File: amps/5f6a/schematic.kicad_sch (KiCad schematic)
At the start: 64 parts, among them T3 2R sec

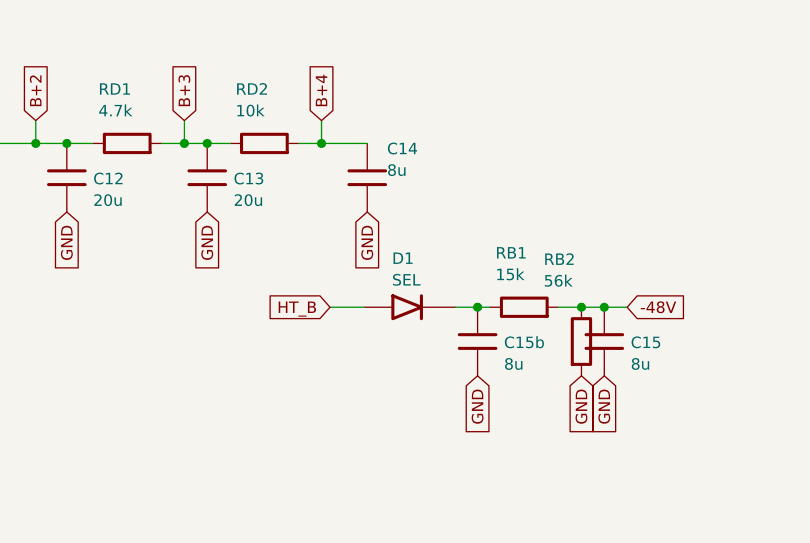
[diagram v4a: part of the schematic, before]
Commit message: Fix: 17 bias rectifiers and six HT diodes drawn backwards; the 6G6-B and 6G4 bias rows as their drawings show; AA1164 V4 units
Rectifier polarity has no gate. The netlists model every supply as an ideal
source, the sheet-vs-board check treats a two-terminal part as unordered, and
the boards' `cathode:` fields were copied from the sheets. Measured over all
68 diodes on 40 sheets: 18 negative-bias rectifiers had the cathode on the
negative node (a diode that way round would charge the node POSITIVE), and all
six 6G6-B HT diodes pointed away from B+. The printed negative bias on each of
those sheets falsifies the drawn orientation; the nine bias rectifiers already
right (AA1164, AA864, AB165, B15N, DR103, JTM100, M1959, M2204, 6G6-B) show
the idiom. Flipped: 5E4-A, 5E5-A, 5E6-A, 5F10, 5F4, 5F6, 5F6-A, 5F8-A, 5G9,
6G2, 6G3, 6G4, 6G5, AA964, AB763, AB763 Super, AB763 Twin, JTM45 (the
M1987's is with the Marshall board repair) and the 6G6-B's DR1-DR6. The
5F8-A board, which had copied its sheet, has the band moved to the tap side;
the other boards' bands are with the board-repair wave. A gate is next.

6G6-B bias. E-FB (6431x3364): the 1K 1W rises from TR1's SECOND secondary
terminal, a bias tap between the upper HT end and the grounded centre tap,
to the diode's + end. The sheet fed the diode from the HT end with the 1K
after it. T1 now carries its tap pin and the row reads tap -> 1K -> diode ->
-54 V. (The triage had read "HT end"; the native crop shows the tap.)

6G4 bias. A-FJ, read natively: tap -> rectifier -> 8 uF -> 10K -> the -55 V
node, which carries a second 8 uF and the 56K to ground as a bleeder. The
sheet fed the rectifier from an HT end, drew the 56K in series and carried
one capacitor. CBIAS2 joins the parts list, and RBIAS1's role now says
bleeder.

AA1164 V4. The K-FD sheet prints the phase inverter 7/6/8 and the tremolo
oscillator 2/1/3 (5554x4346); the sheet had them the other way round.

Gates: check_schematics 40/0 (+selftest), verify_schematic_nets 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
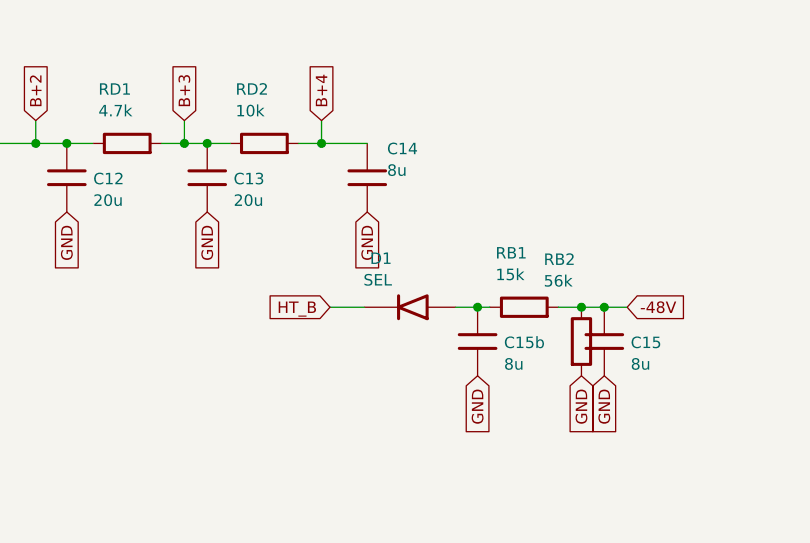
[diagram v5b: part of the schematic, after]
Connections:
- net HT_B: now also D1.2 (K); no longer D1.1 (A)
- net at C15b.1, RB1.1: now also D1.1 (A); no longer D1.2 (K)
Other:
- moved on the sheet: D1
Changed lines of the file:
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@@
   (wire (pts (xy 131.709 142.278) (xy 135.519 142.278))
     (stroke (width 0) (type default)))
-  (symbol (lib_id "cx:DIODE_SS") (at 140.599 142.278 0) (unit 1)
+  (symbol (lib_id "cx:DIODE_SS") (at 140.599 142.278 180) (unit 1)
     (in_bom yes) (on_board yes)
     (property "Reference" "D1" (at 138.599 136.878 0) (effects (font (size 1.27 1.27)) (justify left)))

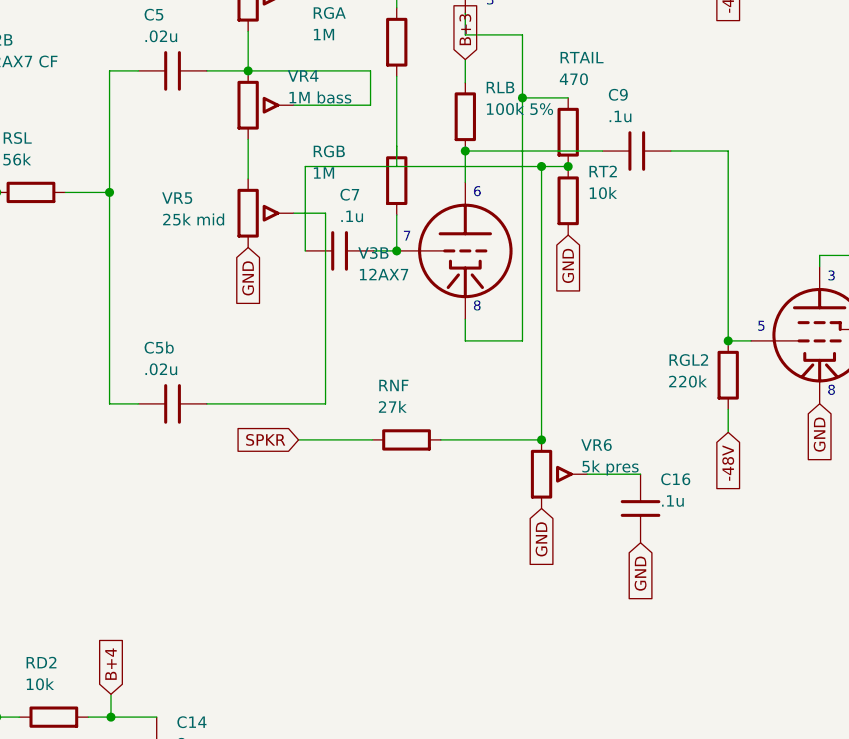
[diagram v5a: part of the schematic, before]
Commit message: Fix: 5F6-A tail returns through the feedback/presence node, not to ground, as I-EG draws it; its two printed tail figures are disputed
- I-EG schematic (6412 x 3947, crops (3100,700)-(3800,2400) and
  (5300,700)-(6412,2500)): the 10k (RT2) leaves the tail junction for a
  vertical of its own carrying the 27k feedback resistor from the speaker, the
  V3B grid's .1-200 and the top of the 5k presence track, whose lower lug is
  grounded with its .1-200 wiper cap to ground. I-EG layout (6402 x 3641, crops
  (3380,1380)-(4450,2400), (2419,534)-(4019,2846)): the same node is the 10k's
  top eyelet with the .1/200 cap, joined under the board to the 27k's eyelet and
  the presence lead, separate from the grounded eyelet beside it.
- Netlist: RT2 JPI PRES; RNF PRES 0 27k (the OT secondary is DC ground);
  RPRES PRES 0 5k; C7 GPIB PRES now modelled. It grounded RT2, dropped the two
  returns as "DC-neutral", and said "the printed chart (J +32.5 V = Itail x 10k)
  confirms this reading" -- arithmetic establishing a reading. Gone.
- Sheet: RT2's foot runs straight down to the node; RNF, VR6 and C7 moved off J
  onto it (C7 now hangs below the V3B grid). sch_map element_pins RPRES =
  VR6.1/VR6.3.
- Board: RT2.b no longer drops to the bus; it carries RNF.b, VR6.lug3 and C7.b.
  C7 is placed on the board at [0,22]-[0,23], as the factory board places it
  (it was absent: a sheet-only row); RPRES declared netlist_unplaced. The
  factory board also mounts the 27k beside the 10k; with no free eyelet pair it
  stays drawn at the speaker jacks, and the caption and BOM notes now say so
  (they called it chassis wiring).
- Chart: with the drawn tail KPI 32.2 -> 43.7 V and JPI 30.7 -> 42.3 V against
  printed 34 / 32.5. The printed plates imply 3.38 mA; x 10k = 33.8 V fits only
  a grounded foot, and the chart is figure for figure the 5F6's, whose 10k is
  grounded. Both nodes are disputed with that arithmetic, not force-fitted.
  PRES added as informational (12.6 V).
- VERIFIED facts cha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
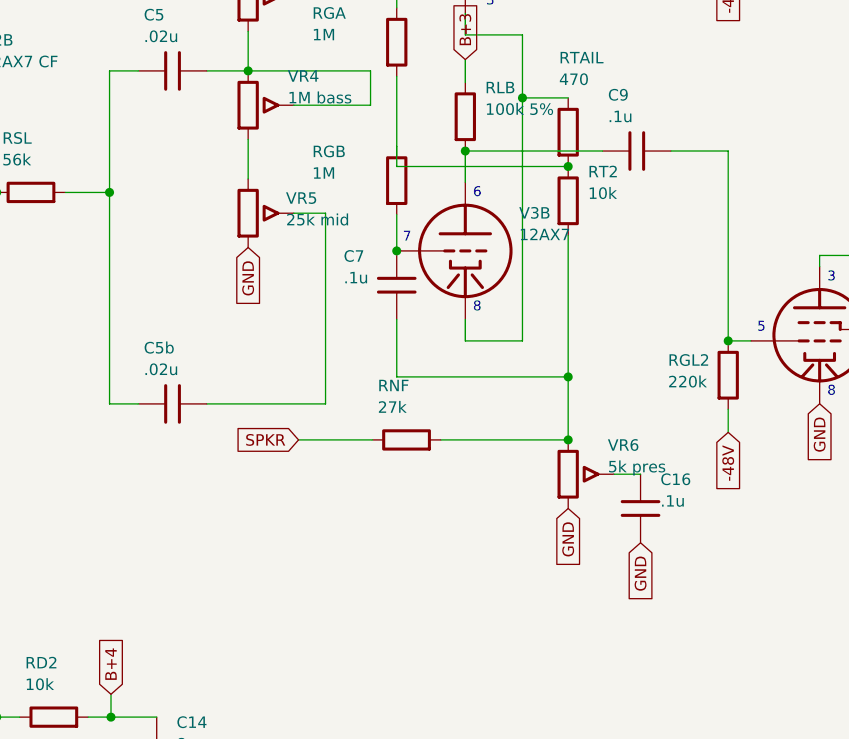
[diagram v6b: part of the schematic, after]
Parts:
- removed C15: 8u, symbol cx:C
- removed C16: .1u, symbol cx:C
- removed RGL1, RGL2: 220k, symbol cx:R
- added C8, C9: .1u, symbol cx:C
- added RB2: 56k, symbol cx:R
- added VR6: 5k pres, symbol cx:POT
- C15: renamed from RB2; value 56k -> 8u; symbol cx:R -> cx:C
- C16: renamed from VR6; value 5k pres -> .1u; symbol cx:POT -> cx:C
- RGL1: renamed from V4; value 5881 -> 220k; symbol cx:PENTODE -> cx:R
- RGL2: renamed from V5; value 5881 -> 220k; symbol cx:PENTODE -> cx:R
- V4: renamed from C8; value .1u -> 5881; symbol cx:C -> cx:PENTODE
- V5: renamed from C9; value .1u -> 5881; symbol cx:C -> cx:PENTODE
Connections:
- net -48V: now also RGL1.2, RGL2.2, RB2.1
- net GND: now also C16.2, V4.4 (K), V5.4 (K), RB2.2, VR6.3; no longer C16.3, RGL1.4 (K), RGL2.4 (K), RT2.2
- net at RS2.1: now also V5.3 (G2); no longer RGL2.3 (G2)
- net at RLB.2, V3B.1 (P): now also C9.1; no longer V5.1
- net at V5.2 (G1): now also RGL2.1, C9.2; no longer RGL2.2 (G1)
- net at RLA.2, V3A.1 (P): now also C8.1; no longer V4.1
- net at V4.2 (G1): now also RGL1.1, C8.2; no longer RGL1.2 (G1)
- net at T3.1 (PRI_A): now also V4.1 (P); no longer RGL1.1 (P)
- net at RS1.1: now also V4.3 (G2); no longer RGL1.3 (G2)
- net at RGA.2, RGB.1, RT2.1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: no longer C16.1, C7.1, RNF.2
- net at T3.3 (PRI_B): now also V5.1 (P); no longer RGL2.1 (P)
- net at RGB.2, V3B.2 (G): now also C7.1; no longer C7.2
- new net: C7.2, RNF.2, RT2.2, VR6.1
- new net: C16.1, VR6.2 (W)
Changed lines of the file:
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@@
   (symbol (lib_id "cx:POT") (at 146.009 68.088 0) (unit 1)
     (in_bom yes) (on_board yes)
-    (property "Reference" "VR5" (at 136.437 66.448 0) (effects (font (size 1.27 1.27)) (justify left)))
-    (property "Value" "25k mid" (at 136.437 68.848 0) (effects (font (size 1.27 1.27)) (justify left))))
+    (property "Reference" "VR5" (at 150.211 66.448 0) (effects (font (size 1.27 1.27)) (justify left)))
+    (property "Value" "25k mid" (at 150.211 68.848 0) (effects (font (size 1.27 1.27)) (justify left))))
   (global_label "GND" (shape input) (at 146.009 71.898 270)
     (effects (font (size 1.27 1.27)) (justify right)))
@@
   (symbol (lib_id "cx:TRIODE") (at 170.139 72.278 0) (unit 1)
     (in_bom yes) (on_board yes)
-    (property "Reference" "V3B" (at 158.234 72.558 0) (effects (font (size 1.27 1.27)) (justify left)))
-    (property "Value" "12AX7" (at 158.234 74.958 0) (effects (font (size 1.27 1.27)) (justify left)))
-    (property "Basing_unit" "1" (at 158.234 77.358 0) (effects (font (size 1.27 1.27)) hide)))
+    (property "Reference" "V3B" (at 176.119 68.098 0) (effects (font (size 1.27 1.27)) (justify left)))
+    (property "Value" "12AX7" (at 176.119 70.498 0) (effects (font (size 1.27 1.27)) (justify left)))
+    (property "Basing_unit" "1" (at 176.119 72.898 0) (effects (font (size 1.27 1.27)) hide)))
   (wire (pts (xy 170.139 30.658) (xy 170.139 27.178))
     (stroke (width 0) (type default)))
@@
     (property "Reference" "RT2" (at 183.769 63.508 0) (effects (font (size 1.27 1.27)) (justify left)))
     (property "Value" "10k" (at 183.769 65.908 0) (effects (font (size 1.27 1.27)) (justify left))))
-  (global_label "GND" (shape input) (at 181.569 70.518 270)
-    (effects (font (size 1.27 1.27)) (justify right)))
   (wire (pts (xy 162.519 38.278) (xy 162.519 45.278))
     (stroke (width 0) (type default)))
@@
   (wire (pts (xy 162.519 60.658) (xy 162.519 62.898))
     (stroke (width 0) (type default)))
-  (wire (pts (xy 162.519 62.898) (xy 178.609 62.898))
-    (stroke (width 0) (type default)))
-  (wire (pts (xy 178.609 62.898) (xy 181.569 62.898))
+  (wire (pts (xy 162.519 62.898) (xy 181.569 62.898))
     (stroke (width 0) (type default)))
   (wire (pts (xy 162.519 72.278) (xy 162.519 68.278))
@@
     (property "Reference" "RGB" (at 153.119 61.268 0) (effects (font (size 1.27 1.27)) (justify left)))
     (property "Value" "1M" (at 153.119 63.668 0) (effects (font (size 1.27 1.27)) (justify left))))
-  (symbol (lib_id "cx:C") (at 156.169 72.278 90) (unit 1)
+  (symbol (lib_id "cx:C") (at 162.519 76.088 0) (unit 1)
     (in_bom yes) (on_board yes)
-    (property "Reference" "C7" (at 156.169 66.078 270) (effects (font (size 1.27 1.27)) (justify left)))
-    (property "Value" ".1u" (at 156.169 68.478 270) (effects (font (size 1.27 1.27)) (justify left))))
-  (wire (pts (xy 159.979 72.278) (xy 162.519 72.278))
+    (property "Reference" "C7" (at 156.619 72.888 0) (effects (font (size 1.27 1.27)) (justify left)))
+    (property "Value" ".1u" (at 156.619 75.288 0) (effects (font (size 1.27 1.27)) (justify left))))
+  (wire (pts (xy 162.519 79.898) (xy 162.519 86.278))
     (stroke (width 0) (type default)))
-  (wire (pts (xy 152.359 72.278) (xy 152.359 72.278))
+  (wire (pts (xy 162.519 86.278) (xy 181.569 86.278))
     (stroke (width 0) (type default)))
-  (wire (pts (xy 152.359 72.278) (xy 152.359 62.898))
+  (wire (pts (xy 181.569 70.518) (xy 181.569 86.278))
     (stroke (width 0) (type default)))
-  (wire (pts (xy 152.359 62.898) (xy 162.519 62.898))
+  (wire (pts (xy 181.569 86.278) (xy 181.569 93.278))
     (stroke (width 0) (type default)))
-  (junction (at 178.609 62.898) (diameter 1.001) (color 0 0 0 0))
-  (wire (pts (xy 178.609 62.898) (xy 178.609 93.278))
-    (stroke (width 0) (type default)))
-  (junction (at 178.609 93.278) (diameter 1.001) (color 0 0 0 0))
+  (junction (at 181.569 86.278) (diameter 1.001) (color 0 0 0 0))
+  (junction (at 181.569 93.278) (diameter 1.001) (color 0 0 0 0))
   (symbol (lib_id "cx:R") (at 163.609 93.278 90) (unit 1)
     (in_bom yes) (on_board yes)
     (property "Reference" "RNF" (at 160.409 87.278 270) (effects (font (size 1.27 1.27)) (justify left)))
     (property "Value" "27k" (at 160.409 89.678 270) (effects (font (size 1.27 1.27)) (justify left))))
-  (wire (pts (xy 167.419 93.278) (xy 178.609 93.278))
+  (wire (pts (xy 167.419 93.278) (xy 181.569 93.278))
     (stroke (width 0) (type default)))
   (wire (pts (xy 151.609 93.278) (xy 159.799 93.278))
@@
   (global_label "SPKR" (shape input) (at 151.609 93.278 180)
     (effects (font (size 1.27 1.27)) (justify right)))
-  (symbol (lib_id "cx:POT") (at 178.609 97.088 0) (unit 1)
+  (symbol (lib_id "cx:POT") (at 181.569 97.088 0) (unit 1)
     (in_bom yes) (on_board yes)
-    (property "Reference" "VR6" (at 183.009 93.888 0) (effects (font (size 1.27 1.27)) (justify left)))
-    (property "Value" "5k pres" (at 183.009 96.288 0) (effects (font (size 1.27 1.27)) (justify left))))
-  (global_label "GND" (shape input) (at 178.609 100.898 270)
+    (property "Reference" "VR6" (at 185.969 93.888 0) (effects (font (size 1.27 1.27)) (justify left)))
+    (property "Value" "5k pres" (at 185.969 96.288 0) (effects (font (size 1.27 1.27)) (justify left))))
+  (global_label "GND" (shape input) (at 181.569 100.898 270)
     (effects (font (size 1.27 1.27)) (justify right)))
-  (wire (pts (xy 183.689 97.088) (xy 189.609 97.088))
+  (wire (pts (xy 186.649 97.088) (xy 189.609 97.088))
     (stroke (width 0) (type default)))
   (symbol (lib_id "cx:C") (at 189.609 100.898 0) (unit 1)
